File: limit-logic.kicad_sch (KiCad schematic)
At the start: 6 parts, among them U17005 4043, U17006 4043, U17007 4078

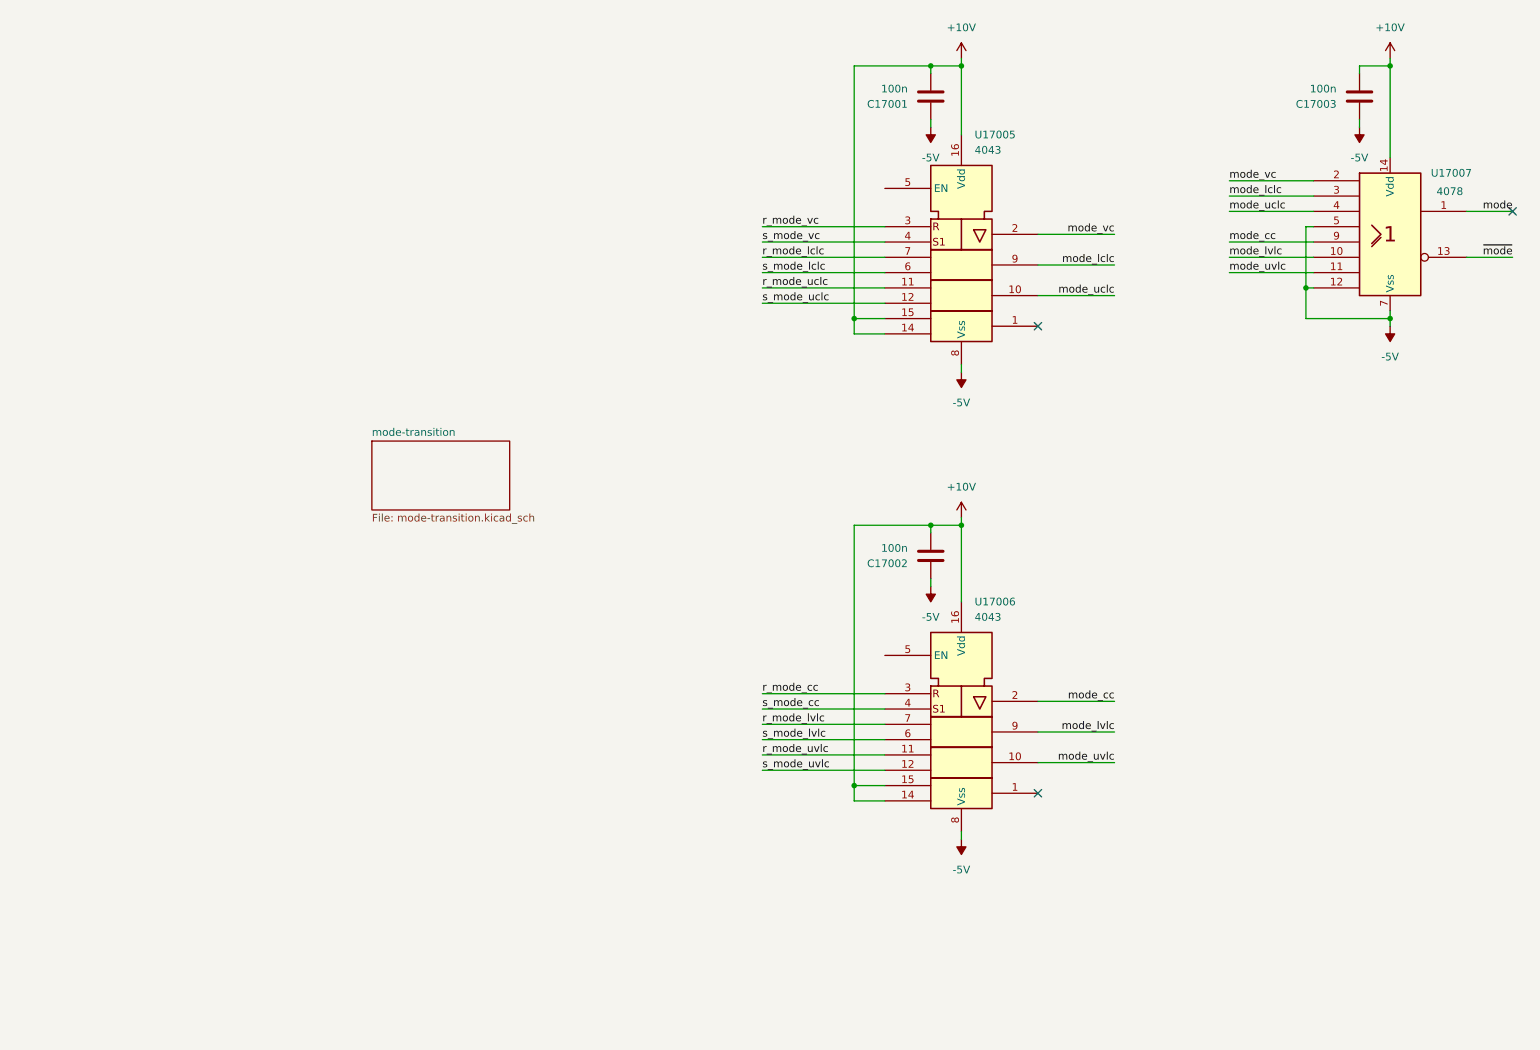
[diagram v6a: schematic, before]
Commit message: add limit-logic pull ups for tristate of mode latches
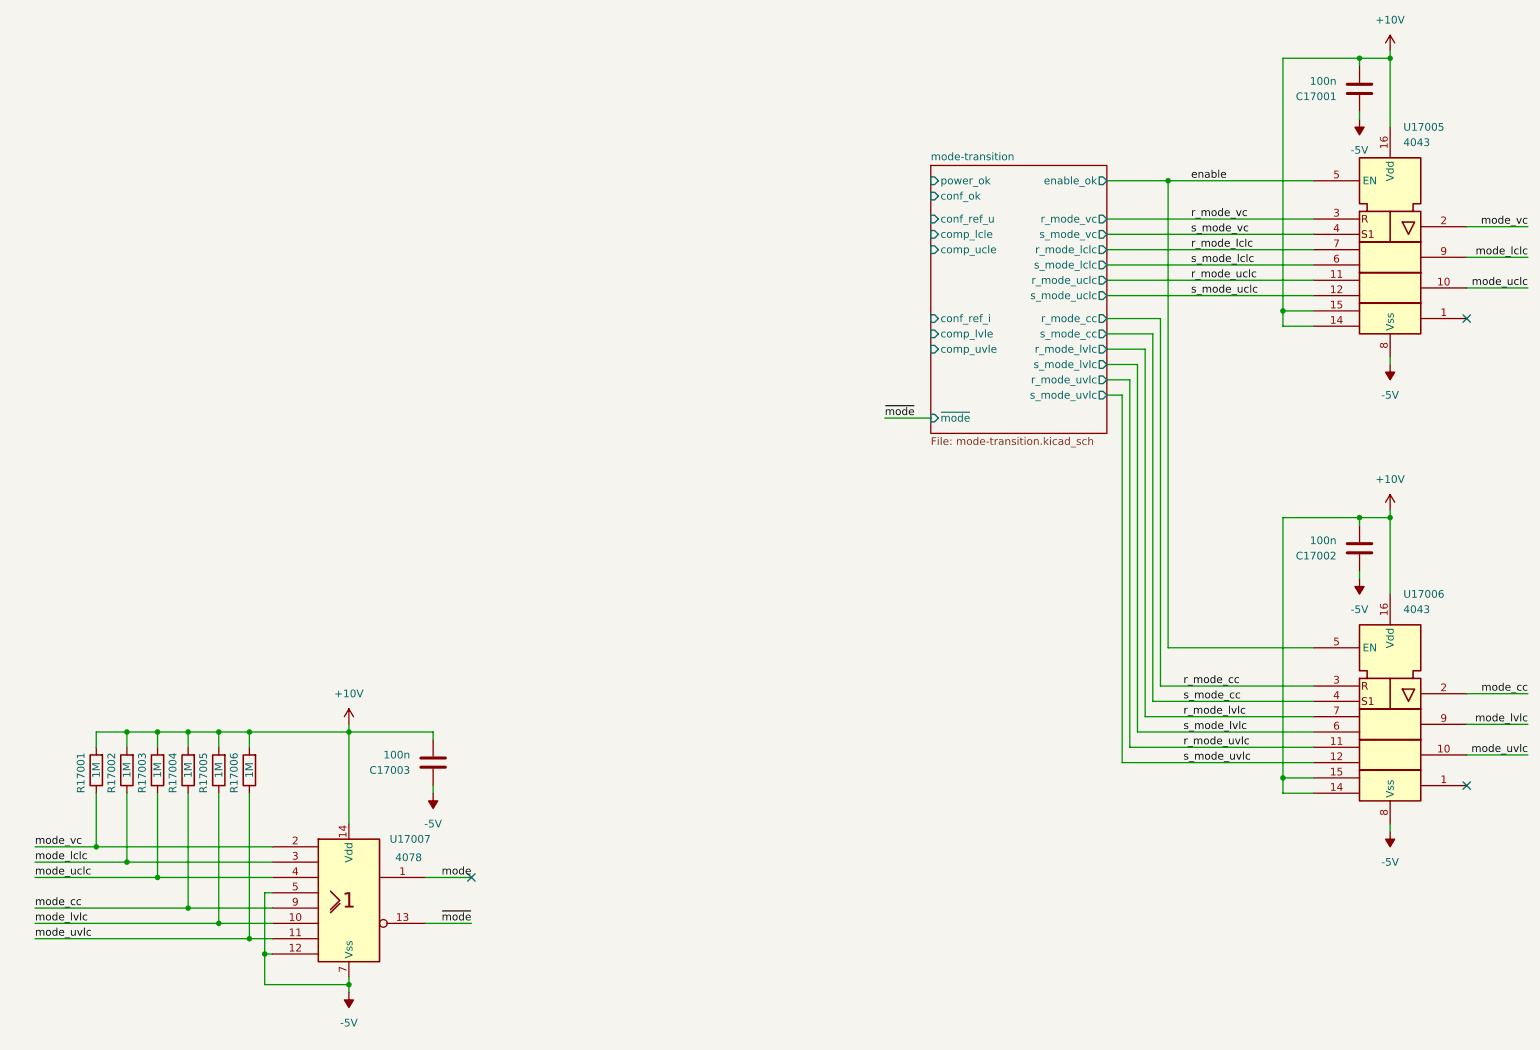
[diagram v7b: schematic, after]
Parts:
- added R17001, R17002, R17003, R17004, R17005, R17006: 1M, Resistor_SMD:R_1210_3225Metric_Pad1.30x2.65mm_HandSolder, symbol pss:R
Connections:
- net +10V: now also R17001.2, R17002.2, R17003.2, R17004.2, R17005.2, R17006.2
- net mode_cc: now also R17004.1
- net mode_lclc: now also R17002.1
- net mode_lvlc: now also R17005.1
- net mode_uclc: now also R17003.1
- net mode_uvlc: now also R17006.1
- net mode_vc: now also R17001.1
- net enable: now reaches U17006.5 (EN)
- net enable: now also U17005.5 (EN)
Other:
- sheet mode-transition ports: added comp_lcle, comp_lvle, comp_ucle, comp_uvle, conf_ok, conf_ref_i, conf_ref_u, enable_ok, power_ok, r_mode_cc, r_mode_lclc, r_mode_lvlc, r_mode_uclc, r_mode_uvlc, r_mode_vc, s_mode_cc, s_mode_lclc, s_mode_lvlc, s_mode_uclc, s_mode_uvlc, s_mode_vc, ~{mode}; removed none
- moved on the sheet: C17001, C17002, C17003, U17005, U17006, U17007

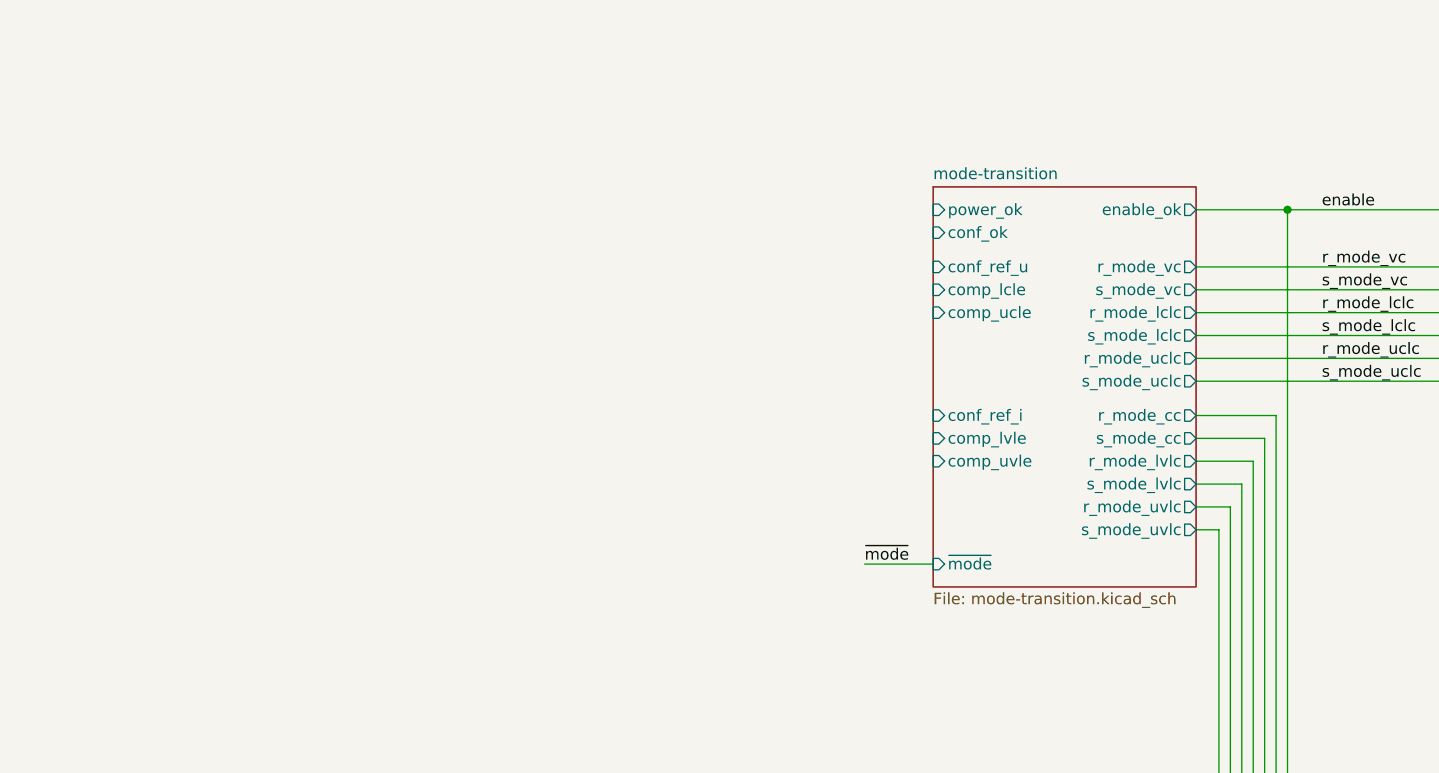
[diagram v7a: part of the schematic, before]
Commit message: add limit-logic compare-logic hierachical sheet and hirarchy connectors
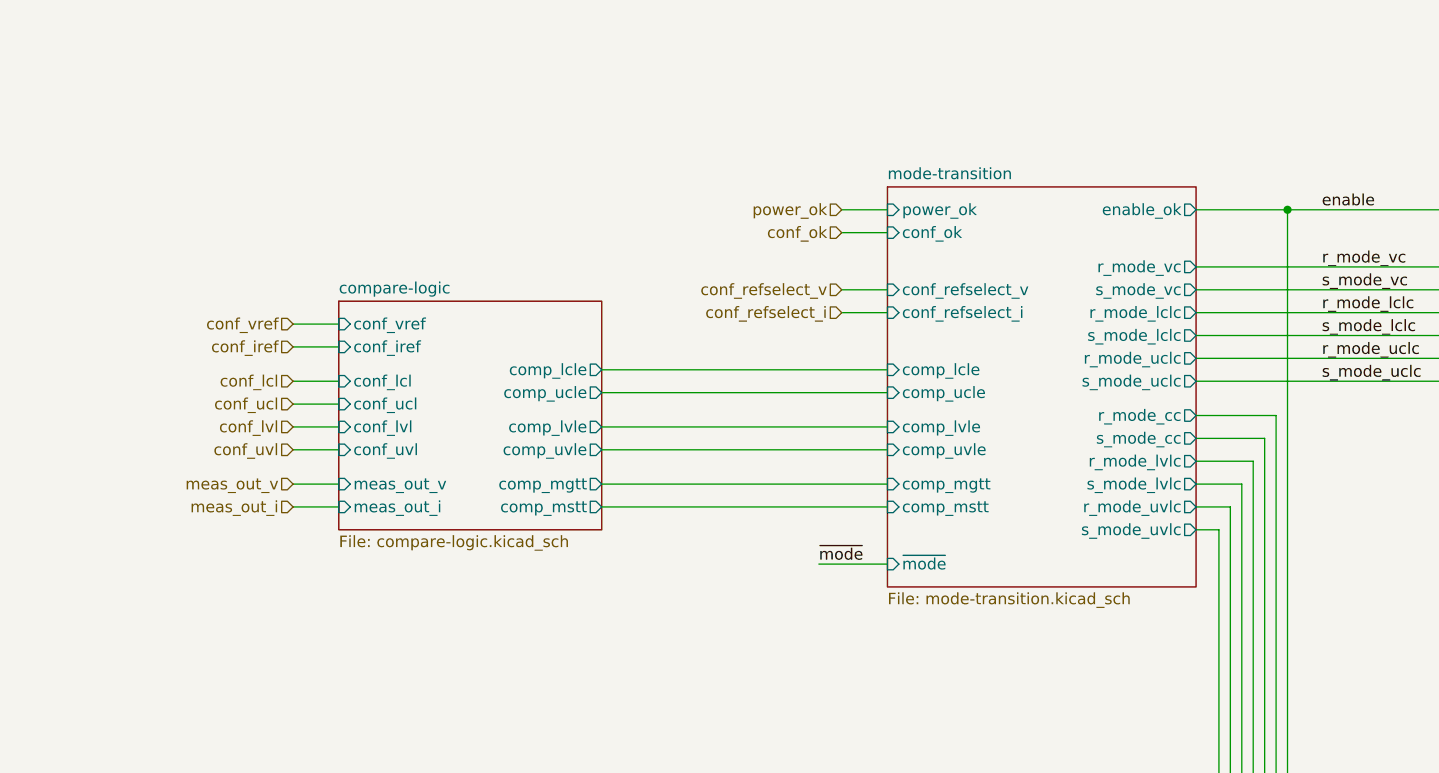
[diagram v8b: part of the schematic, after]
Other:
- added sheet compare-logic (compare-logic.kicad_sch)
- sheet mode-transition ports: added comp_mgtt, comp_mstt, conf_refselect_i, conf_refselect_v; removed conf_ref_i, conf_ref_u
